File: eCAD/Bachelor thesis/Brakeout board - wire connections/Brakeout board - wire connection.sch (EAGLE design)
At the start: 6 parts, among them IC1 VEML7700-TR

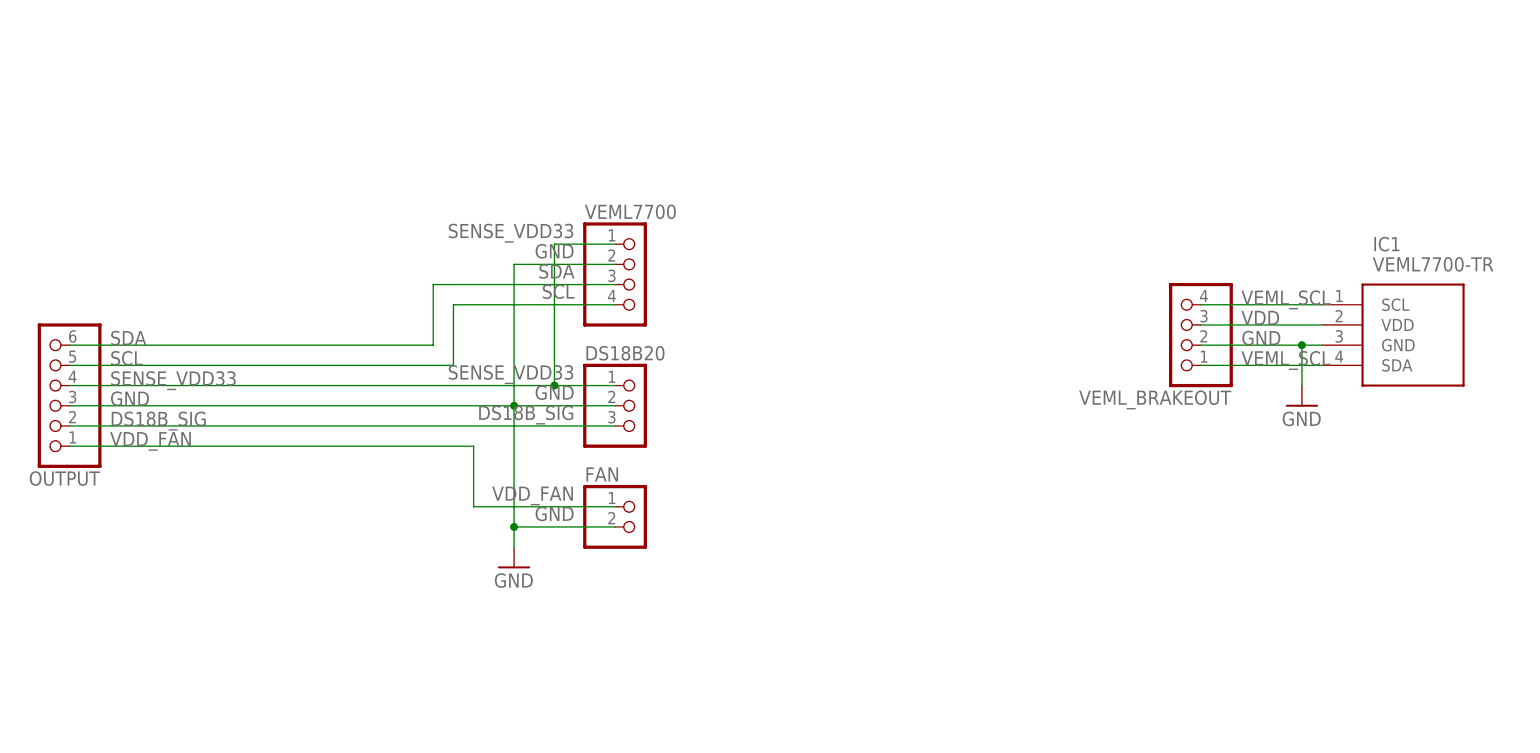
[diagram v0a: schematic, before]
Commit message: Separated wire connection board and VEM7700 brakeout board, to VEML7700 board added R and C acording to datasheet
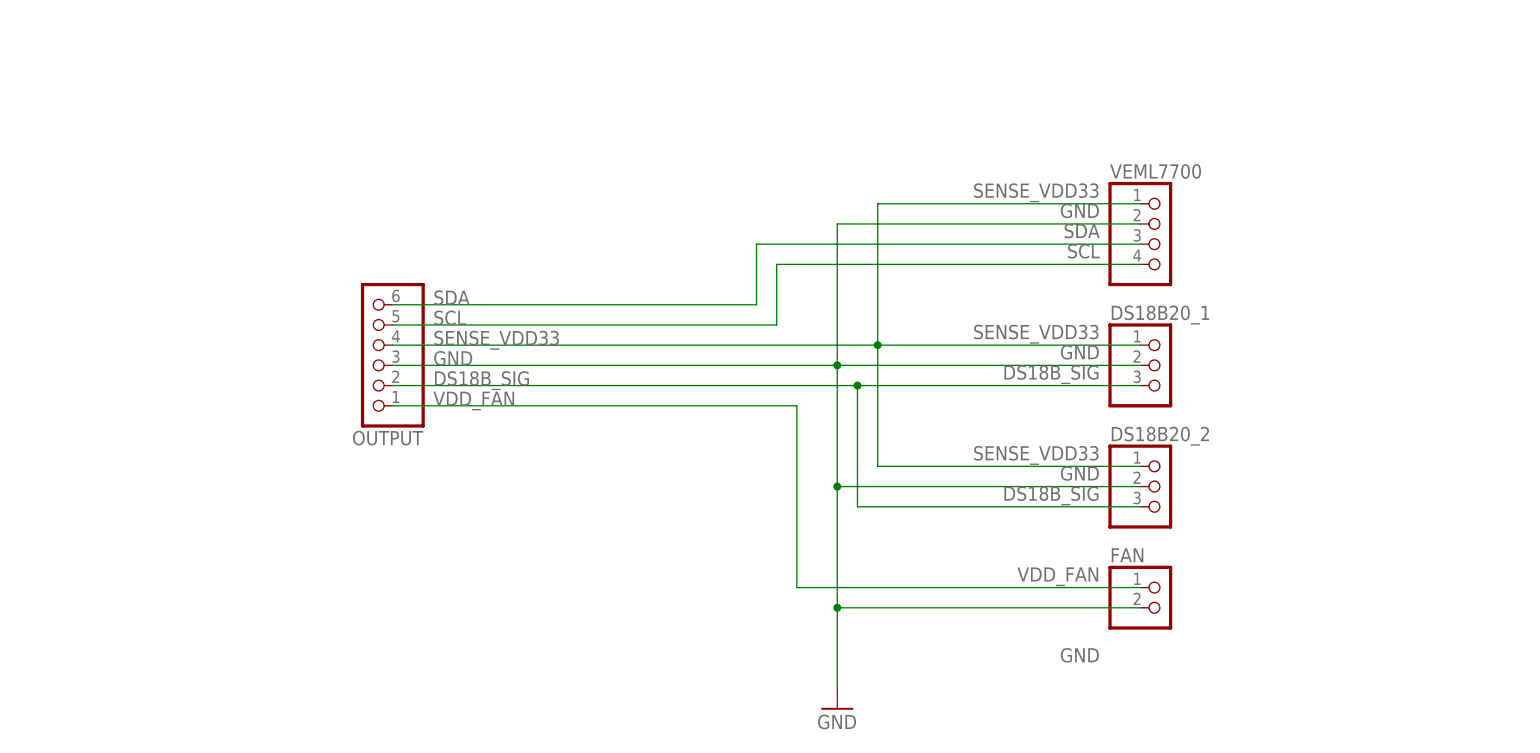
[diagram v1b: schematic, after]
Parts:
- removed DS18B20: (no value), pinhead:PINHD-1X3
- removed IC1: VEML7700-TR, 1-component-search:VEML7700-TR
- removed VEML_BRAKEOUT: (no value), pinhead:PINHD-1X4
- added DS18B20_1, DS18B20_2: (no value), pinhead:PINHD-1X3
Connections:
- removed net VDD: IC1.VDD, VEML_BRAKEOUT.3
- removed net VEML_SCL: IC1.SCL, IC1.SDA, VEML_BRAKEOUT.1, VEML_BRAKEOUT.4
- net DS18B_SIG: now also DS18B20_1.3, DS18B20_2.3; no longer DS18B20.3
- net GND: now also DS18B20_1.2, DS18B20_2.2; no longer DS18B20.2, IC1.GND, VEML_BRAKEOUT.2
- net SENSE_VDD33: now also DS18B20_1.1, DS18B20_2.1; no longer DS18B20.1
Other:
- moved on the sheet: FAN, OUTPUT, VEML7700

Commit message: Final touches
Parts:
- added I2C_RES: (no value), pinhead:PINHD-1X4
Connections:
- net GND: now also I2C_RES.2
- net SCL: now also I2C_RES.4
- net SDA: now also I2C_RES.3
- net SENSE_VDD33: now also I2C_RES.1
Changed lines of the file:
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@@
 <part name="GND1" library="supply1" library_urn="urn:adsk.eagle:library:371" deviceset="GND" device=""/>
 <part name="DS18B20_2" library="pinhead" library_urn="urn:adsk.eagle:library:325" deviceset="PINHD-1X3" device="" package3d_urn="urn:adsk.eagle:package:22458/2"/>
+<part name="I2C_RES" library="pinhead" library_urn="urn:adsk.eagle:library:325" deviceset="PINHD-1X4" device="" package3d_urn="urn:adsk.eagle:package:22407/2"/>
 </parts>
 <sheets>
@@
 <attribute name="VALUE" x="171.45" y="66.04" size="1.778" layer="96"/>
 </instance>
+<instance part="I2C_RES" gate="A" x="177.8" y="121.92" smashed="yes">
+<attribute name="NAME" x="171.45" y="130.175" size="1.778" layer="95"/>
+<attribute name="VALUE" x="171.45" y="114.3" size="1.778" layer="96"/>
+</instance>
 </instances>
 <busses>
@@
 <net name="SENSE_VDD33" class="0">
 <segment>
+<pinref part="I2C_RES" gate="A" pin="1"/>
+<wire x1="142.24" y1="127" x2="175.26" y2="127" width="0.1524" layer="91"/>
+<label x="170.18" y="129.54" size="1.778" layer="95" rot="R180"/>
 <wire x1="142.24" y1="91.44" x2="142.24" y2="109.22" width="0.1524" layer="91"/>
 <pinref part="VEML7700" gate="A" pin="1"/>
@@
 <wire x1="142.24" y1="76.2" x2="142.24" y2="91.44" width="0.1524" layer="91"/>
 <label x="170.18" y="78.74" size="1.778" layer="95" rot="R180"/>
+<wire x1="142.24" y1="127" x2="142.24" y2="109.22" width="0.1524" layer="91"/>
+<junction x="142.24" y="109.22"/>
 </segment>
 </net>
@@
 <junction x="137.16" y="73.66"/>
 <label x="170.18" y="76.2" size="1.778" layer="95" rot="R180"/>
+<pinref part="I2C_RES" gate="A" pin="2"/>
+<wire x1="137.16" y1="124.46" x2="175.26" y2="124.46" width="0.1524" layer="91"/>
+<label x="170.18" y="127" size="1.778" layer="95" rot="R180"/>
+<wire x1="137.16" y1="124.46" x2="137.16" y2="106.68" width="0.1524" layer="91"/>
+<junction x="137.16" y="106.68"/>
 </segment>
 </net>
@@
 <net name="SDA" class="0">
 <segment>
-<pinref part="VEML7700" gate="A" pin="3"/>
-<wire x1="127" y1="104.14" x2="175.26" y2="104.14" width="0.1524" layer="91"/>
+<pinref part="I2C_RES" gate="A" pin="3"/>
+<wire x1="127" y1="121.92" x2="175.26" y2="121.92" width="0.1524" layer="91"/>
+<label x="170.18" y="124.46" size="1.778" layer="95" rot="R180"/>
 <label x="170.18" y="106.68" size="1.778" layer="95" rot="R180"/>
 <pinref part="OUTPUT" gate="A" pin="6"/>
 <wire x1="81.28" y1="96.52" x2="127" y2="96.52" width="0.1524" layer="91"/>
-<wire x1="127" y1="96.52" x2="127" y2="104.14" width="0.1524" layer="91"/>
 <label x="86.36" y="96.52" size="1.778" layer="95"/>
+<wire x1="127" y1="121.92" x2="127" y2="104.14" width="0.1524" layer="91"/>
+<pinref part="VEML7700" gate="A" pin="3"/>
+<wire x1="127" y1="104.14" x2="127" y2="96.52" width="0.1524" layer="91"/>
+<wire x1="175.26" y1="104.14" x2="127" y2="104.14" width="0.1524" layer="91"/>
+<junction x="127" y="104.14"/>
 </segment>
 </net>
 <net name="SCL" class="0">
 <segment>
+<pinref part="I2C_RES" gate="A" pin="4"/>
+<wire x1="129.54" y1="119.38" x2="175.26" y2="119.38" width="0.1524" layer="91"/>
+<label x="170.18" y="121.92" size="1.778" layer="95" rot="R180"/>
 <pinref part="VEML7700" gate="A" pin="4"/>
 <wire x1="129.54" y1="101.6" x2="175.26" y2="101.6" width="0.1524" layer="91"/>
@@
 <wire x1="129.54" y1="93.98" x2="129.54" y2="101.6" width="0.1524" layer="91"/>
 <label x="86.36" y="93.98" size="1.778" layer="95"/>
+<wire x1="129.54" y1="119.38" x2="129.54" y2="101.6" width="0.1524" layer="91"/>
+<junction x="129.54" y="101.6"/>
 </segment>
 </net>
